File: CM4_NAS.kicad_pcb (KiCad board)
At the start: 4 copper layers, 88.5 x 72.5 mm, 30 parts, among them J1 USB_A, J10 Conn_02x07_Odd_Even, J11 Conn_01x03, J13 USB_OTG, J14 USB_select_jmpr, J15 Temp_Sensor, J2 HDMI_header, J3 PCIe_conn, J4 Sata_PWR, J5 PWR_IN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

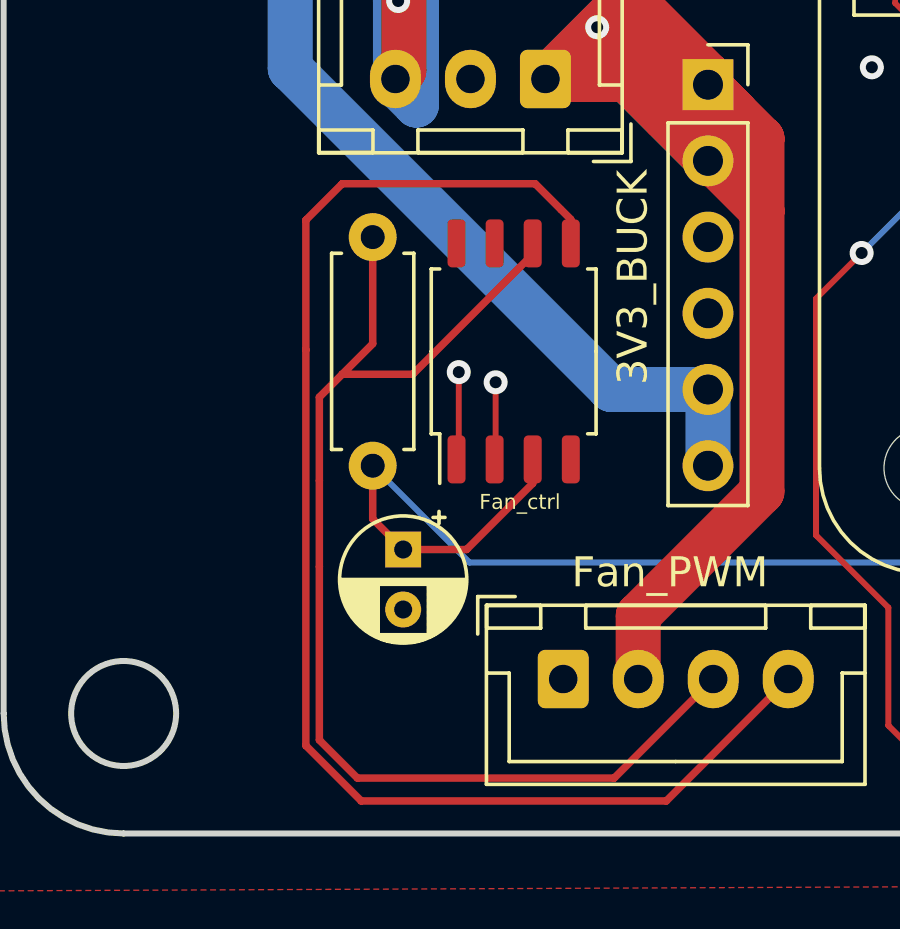
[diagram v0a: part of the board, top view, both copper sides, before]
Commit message: Fixed wrong footprint
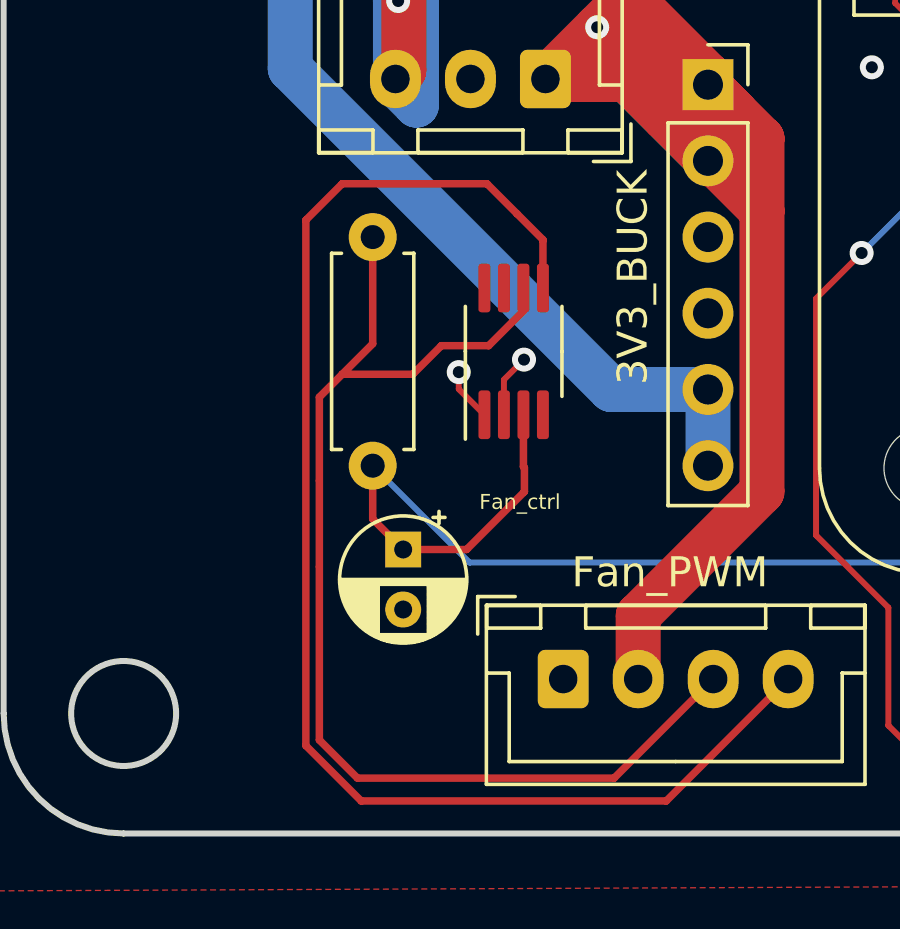
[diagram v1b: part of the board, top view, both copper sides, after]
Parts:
- U6: footprint Package_SO:SOIC-8_5.275x5.275mm_P1.27mm -> Package_SO:MSOP-8_3x3mm_P0.65mm
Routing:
- net /SCL: track 101.3 -> 99.5 mm
- net /+3.3v: track 204.7 -> 205.9 mm
- net /SDA: track 103.2 -> 102.0 mm
- net Net-(J7-Pad3): track 40.9 -> 40.2 mm

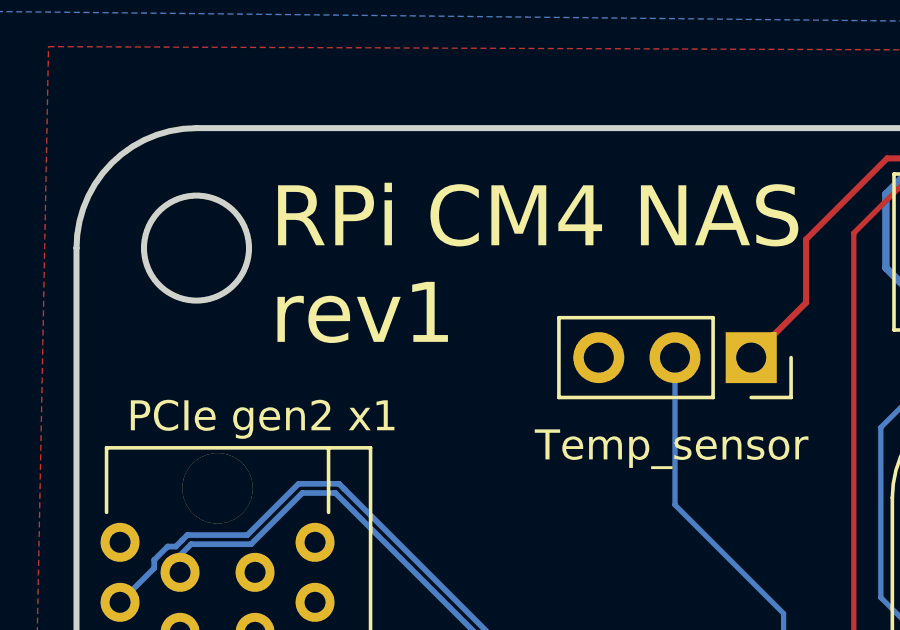
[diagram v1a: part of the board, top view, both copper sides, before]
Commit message: Updated revision on silkscreen
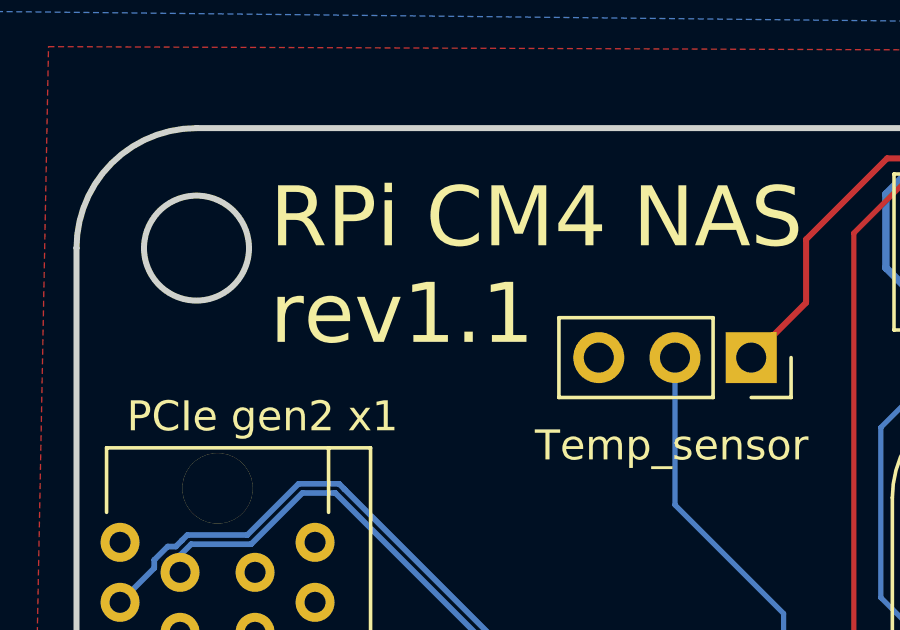
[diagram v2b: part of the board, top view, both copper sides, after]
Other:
- board text added: "RPi CM4 NAS rev1.1"
- board text removed: "RPi CM4 NAS rev1"
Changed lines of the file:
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@@
     (effects (font (size 1 1) (thickness 0.15)))
   )
-  (gr_text "RPi CM4 NAS\nrev1" (at 96.51 73.89) (layer "F.SilkS")
+  (gr_text "RPi CM4 NAS\nrev1.1" (at 96.51 73.89) (layer "F.SilkS")
     (effects (font (size 2 2) (thickness 0.3)) (justify left))
   )

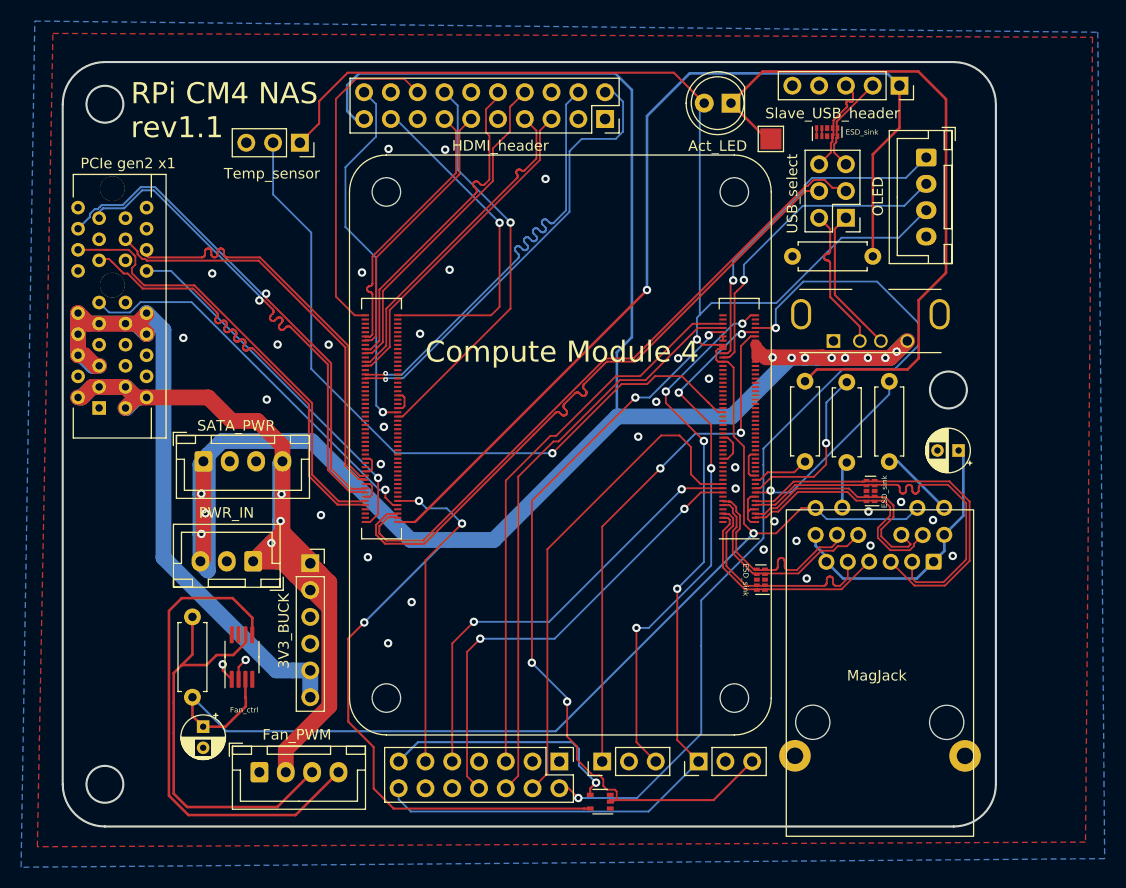
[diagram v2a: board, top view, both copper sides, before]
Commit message: new usb select header
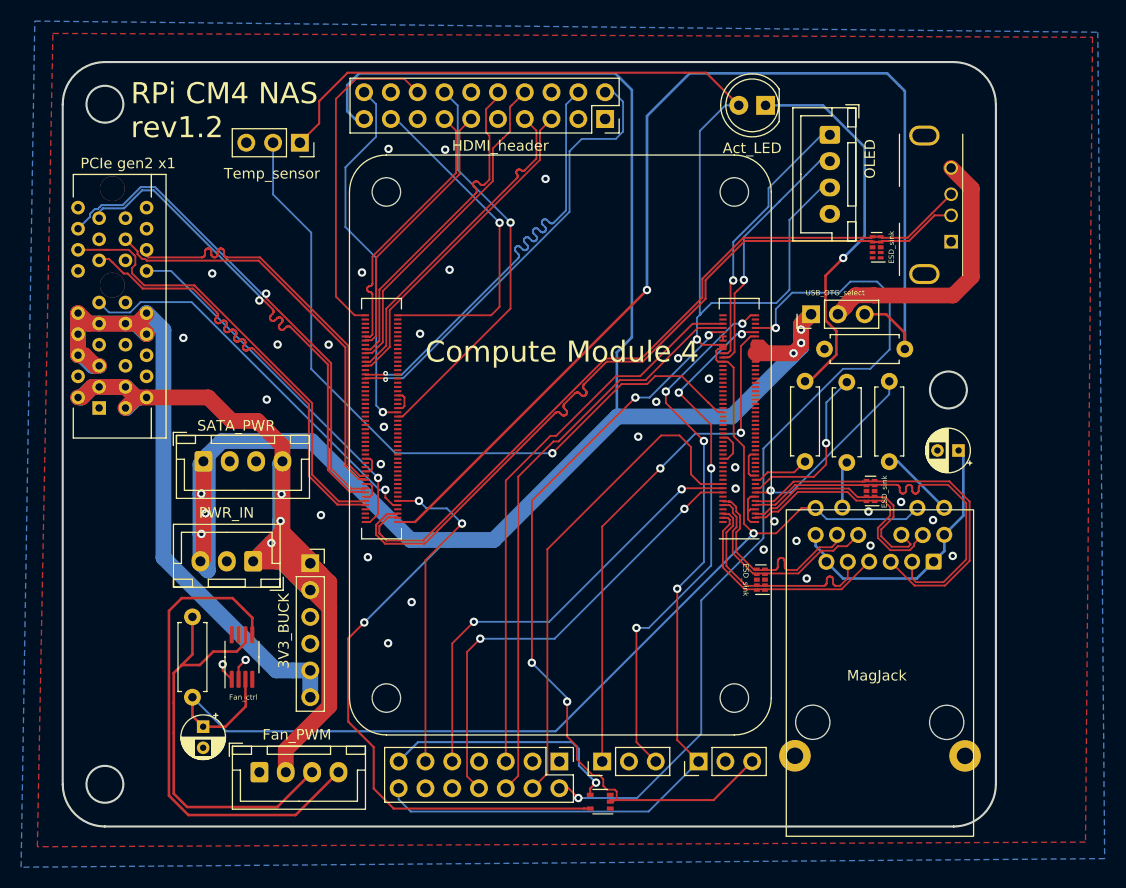
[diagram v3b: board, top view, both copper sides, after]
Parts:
- removed J13: USB_OTG, Connector_PinSocket_2.54mm:PinSocket_1x05_P2.54mm_Vertical
- removed J14: USB_select_jmpr, Connector_PinHeader_2.54mm:PinHeader_2x03_P2.54mm_Vertical
- removed TP1: TestPoint, TestPoint:TestPoint_Pad_2.0x2.0mm
- added J12: Conn_01x03, Connector_PinHeader_2.54mm:PinHeader_1x03_P2.54mm_Vertical, F.Cu at (161.0, 93.2)
- moved J1 14.6 mm to (174.3, 86.3), turned to 90 degrees
- moved U5 11.9 mm to (167.3, 86.9), turned to 180 degrees
- moved J8 9.39 mm to (162.8, 76.2)
- moved R4 9.30 mm to (169.9, 96.5)
- moved D1 3.28 mm to (156.7, 73.4)
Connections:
- J1 pad 1: +5V -> /USB2_VBUS
- J1 pad 2: /Master_USB2_N -> /USB2_N
- J1 pad 3: /Master_USB2_P -> /USB2_P
- U5 pad 4: /Slave_MicroUSB_P -> /USB2_P
- U5 pad 5: /Slave_MicroUSB_N -> /USB2_N
- U5 pad 6: /Slave_MicroUSB_N -> /USB2_N
- U5 pad 7: /Slave_MicroUSB_P -> /USB2_P
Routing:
- net Net-(D1-Pad1): track 65.2 -> 36.7 mm, vias 0 -> 1
- net /USB2_VBUS: track 0.00 -> 25.4 mm
- net /USBOTG_ID: track 92.6 -> 106.6 mm
- net /Master_USB2_P: track 13.9 -> 0.00 mm
- net /Master_USB2_N: track 13.9 -> 0.00 mm
- net +5V: track 242.8 -> 229.3 mm, vias 12 -> 7
- net /USB2_P: track 61.9 -> 74.6 mm
- net /USB2_N: track 61.9 -> 72.0 mm
- net /Slave_MicroUSB_P: track 9.83 -> 0.00 mm
- net /Slave_MicroUSB_N: track 9.59 -> 0.00 mm
- net /SCL: track 99.5 -> 93.0 mm
- net /SDA: track 102.0 -> 95.6 mm
- net /nRPIBOOT: track 86.7 -> 83.1 mm
- net /+3.3v: track 205.9 -> 206.8 mm
- net Net-(U5-Pad2): track 0.77 -> 0.00 mm
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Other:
- board text added: "RPi CM4 NAS rev1.2"
- board text added: "USB_OTG_select"
- board text removed: "RPi CM4 NAS rev1.1"
- board text removed: "Slave_USB_header"
- board text removed: "USB_select"

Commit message: HDMI, silkscreen, gpios...
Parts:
- added D2: LED Red, LED_THT:LED_D5.0mm, F.Cu at (149.5, 73.4)
- added J13: Conn_02x06_Odd_Even, Connector_PinHeader_2.54mm:PinHeader_2x06_P2.54mm_Vertical, F.Cu at (129.3, 75.3)
- added R6: 1k, Resistor_THT:R_Axial_DIN0207_L6.3mm_D2.5mm_P7.62mm_Horizontal, F.Cu at (160.0, 71.6)
- added U7: 74LVC1G07SE-7, Package_TO_SOT_SMD:SOT-353_SC-70-5, F.Cu at (160.6, 88.5)
- J2: footprint CM4:PinSocket_2x10_P2.54mm_Vertical_alternate-pinout -> CM4:HDMI EDAC 690-019-298-412
- R5: value 36K 1% -> 36K
- moved J2 33.3 mm to (108.6, 79.8), turned to 180 degrees
- moved J15 9.18 mm to (108.9, 85.4)
- moved J5 0.27 mm to (108.4, 116.6)
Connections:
- J3 pad A16: /PCIE_RX_N -> /PCIE_RX_P
- J3 pad A17: /PCIE_RX_P -> /PCIE_RX_N
- J3 pad B14: /PCIE_TX_N -> /PCIE_TX_P
- J3 pad B15: /PCIE_TX_P -> /PCIE_TX_N
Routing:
- net /GPIO24: track 0.00 -> 64.8 mm, vias 0 -> 1
- net /+3.3v: track 206.8 -> 271.4 mm, vias 2 -> 3
- net /GPIO14: track 0.00 -> 64.1 mm, vias 0 -> 1
- net /GPIO12: track 0.00 -> 62.5 mm, vias 0 -> 1
- net /GPIO15: track 0.00 -> 55.4 mm, vias 0 -> 1
- net /GPIO18: track 0.00 -> 53.5 mm, vias 0 -> 1
- net /GPIO23: track 0.00 -> 53.1 mm, vias 0 -> 1
- net /GPIO26: track 0.00 -> 49.4 mm, vias 0 -> 1
- net /GPIO3: track 0.00 -> 37.2 mm, vias 0 -> 1
- net /GPIO2: track 0.00 -> 34.9 mm, vias 0 -> 1
- net +12V: track 125.1 -> 151.3 mm, vias 3 -> 13
- net Net-(R6-Pad2): track 0.00 -> 24.2 mm, vias 0 -> 1
- net /HDMI0_SCL: track 31.3 -> 15.2 mm
- net Net-(D2-Pad1): track 0.00 -> 14.5 mm
- net /HDMI0_SDA: track 32.4 -> 18.0 mm, vias 1 -> 2
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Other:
- board text added: "12"
- board text added: "14"
- board text added: "15"
- board text added: "18"
- board text added: "2"
- board text added: "23"
- board text added: "24"
- board text added: "26"
- board text added: "3"
- board text added: "3V3"
- board text added: "5V"
- board text added: "AIN0"
- board text added: "AIN1"
- board text added: "Buff_RUN_PG"
- board text added: "EEPROM_nWP"
- board text added: "GLOBAL_EN"
- board text added: "GND"
- board text added: "GPIOs"
- board text added: "PCIe 2.0 x1"
- board text added: "Pwr_LED"
- board text added: "RPi CM4 NAS rev1.3"
- board text added: "SYNC_IN"
- board text added: "SYNC_OUT"
- board text added: "TV_OUT"
- board text added: "nRPIBOOT"
- board text removed: "HDMI_header"
- board text removed: "PCIe gen2 x1"
- board text removed: "RPi CM4 NAS rev1.2"
